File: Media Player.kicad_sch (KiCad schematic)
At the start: 40 parts, among them J1 PH2.0, J2 MEM2075-00-140-01-A, J3 USB_C_Receptacle_USB2.0_14P, SW1 BOOT, SW2 RESET, SW3 SW_Push, SW4 SW_Push, SW5 SW_Push, SW6 SW_Push, SW7 SW_SPST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

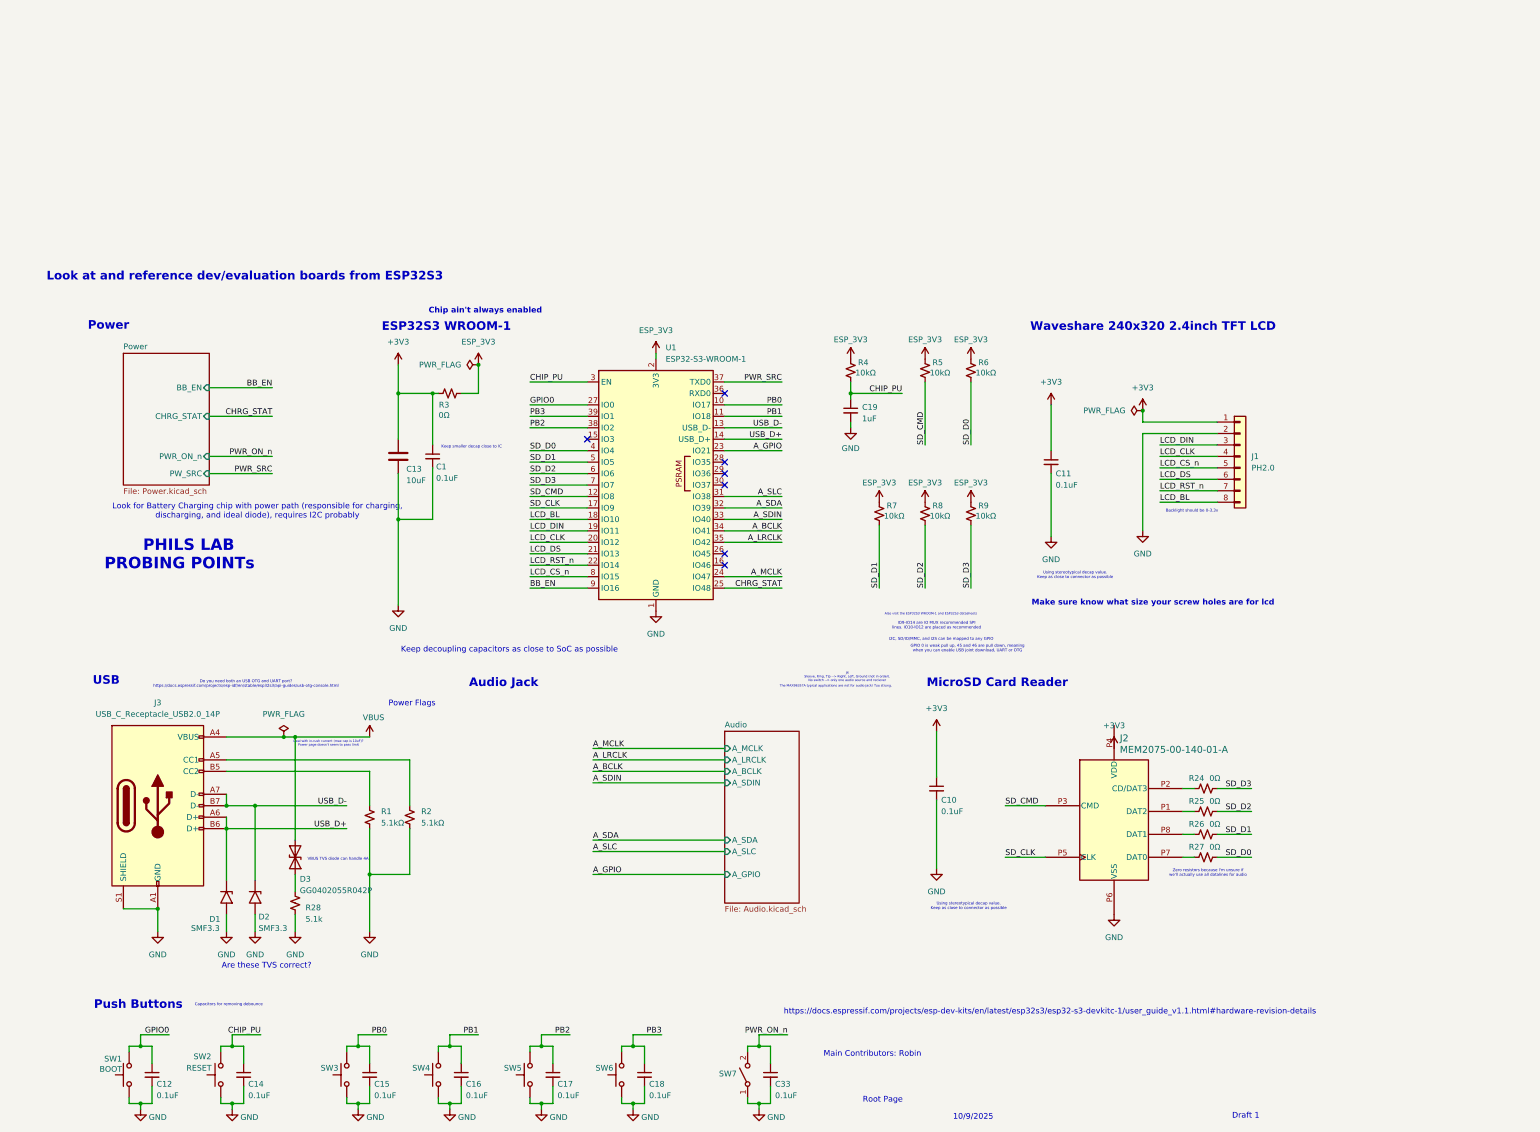
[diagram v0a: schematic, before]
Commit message: Draft 2 Revision 2
Footprints still not all assigned.

Added: Test points, zero resistors, battery voltage monitor IC, PTC and zener surge protection on VBUS, UART connector

Changed: rerouted some signals, removed zener and resistor for reverse pol bat protection
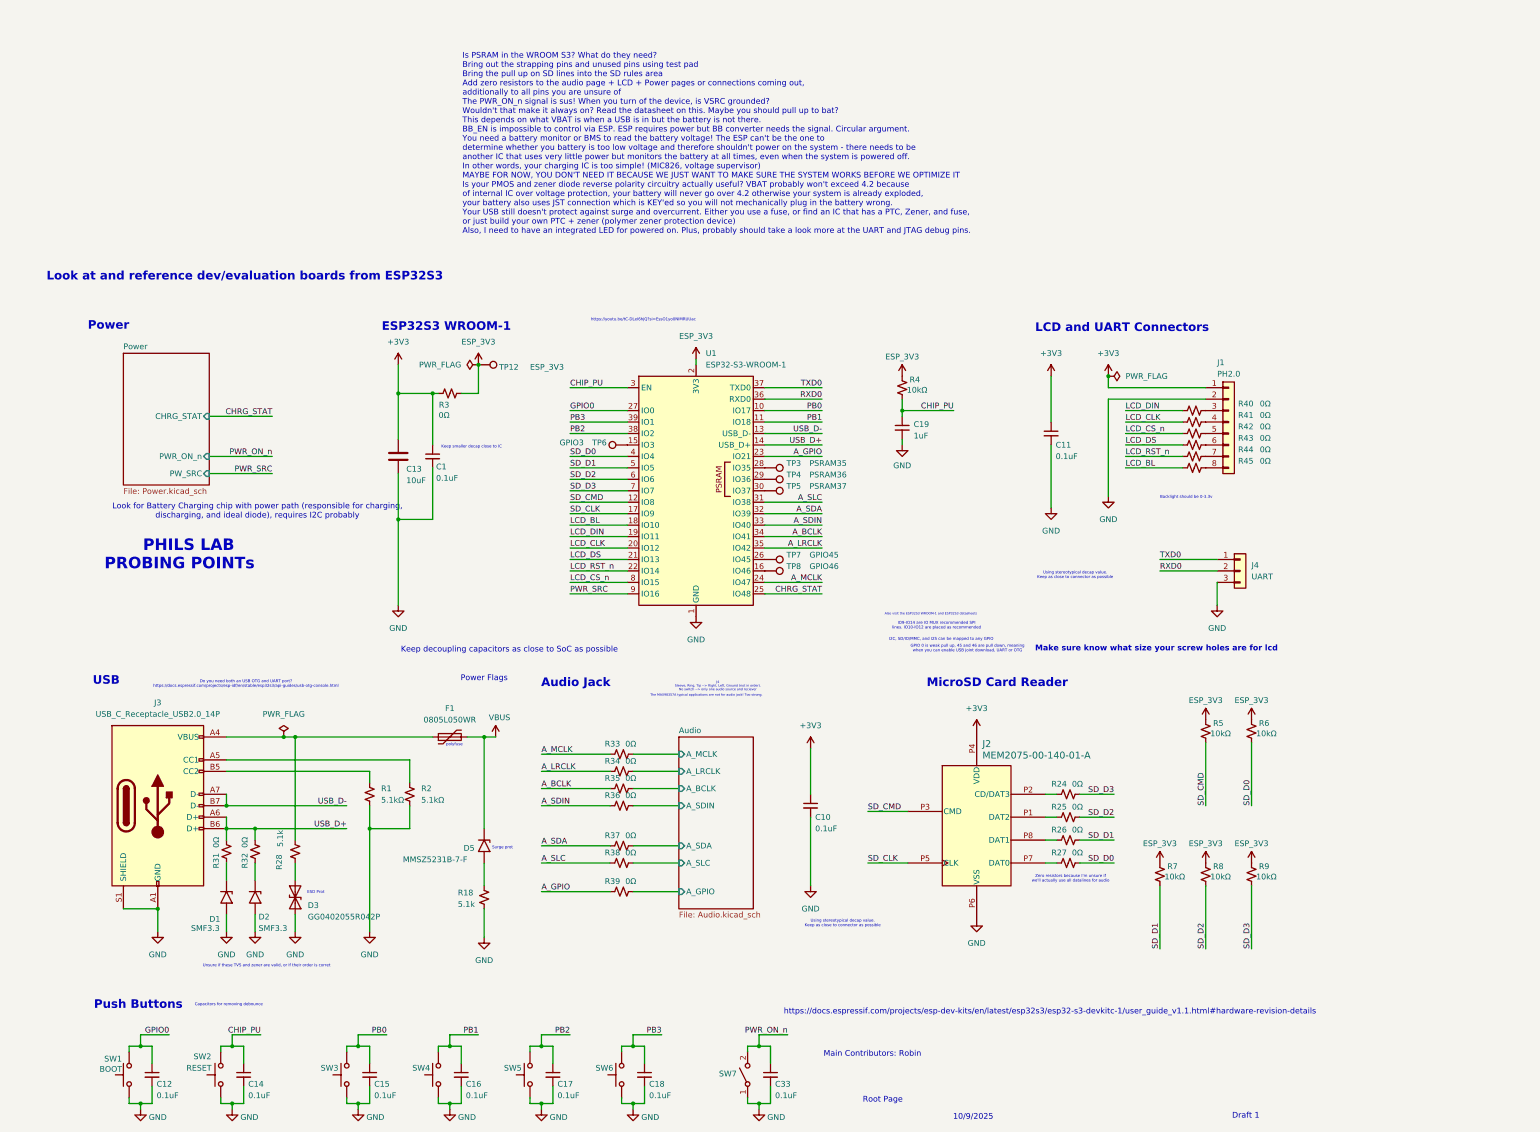
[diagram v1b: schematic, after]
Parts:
- added D5: MMSZ5231B-7-F, Diode_SMD:D_SMF, symbol Diode:SMF33A
- added F1: 0805L050WR, symbol Device:Polyfuse
- added J4: UART, symbol Connector_Generic:Conn_01x03
- added R18: 5.1k, symbol Device:R_Small_US
- added R31, R32, R33, R34, R35, R36, R37, R38, R39, R40, R41, R42, R43, R44, R45: 0Ω, Resistor_SMD:R_0805_2012Metric, symbol Device:R_Small_US
- added TP12: ESP_3V3, symbol Connector:TestPoint
- added TP3: PSRAM35, symbol Connector:TestPoint
- added TP4: PSRAM36, symbol Connector:TestPoint
- added TP5: PSRAM37, symbol Connector:TestPoint
- added TP6: GPIO3, symbol Connector:TestPoint
- added TP7: GPIO45, symbol Connector:TestPoint
- added TP8: GPIO46, symbol Connector:TestPoint
- R28: footprint (none) -> Resistor_SMD:R_0805_2012Metric
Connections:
- net BB_EN is gone; now on net PWR_SRC: U1.9 (IO16)
- net +3V3: now also J2.P4 (VDD)
- net A_BCLK: now also R35.1
- net A_GPIO: now also R39.1
- net A_LRCLK: now also R34.1
- net A_MCLK: now also R33.1
- net A_SDA: now also R37.1
- net A_SDIN: now also R36.1
- net A_SLC: now also R38.1
- net ESP_3V3: now also TP12.1
- net GND: now also D3.1 (A1), J4.3 (Pin_3), R18.2; no longer R28.2
- net LCD_BL: now also R45.1; no longer J1.8 (Pin_8)
- net LCD_CLK: now also R41.1; no longer J1.4 (Pin_4)
- net LCD_CS_n: now also R42.1; no longer J1.5 (Pin_5)
- net LCD_DIN: now also R40.1; no longer J1.3 (Pin_3)
- net LCD_DS: now also R43.1; no longer J1.6 (Pin_6)
- net LCD_RST_n: now also R44.1; no longer J1.7 (Pin_7)
- net PWR_SRC: no longer U1.37 (TXD0)
- net USB_D+: now also R31.2, R32.2; no longer D1.1 (A1)
- net USB_D-: no longer D2.1 (A1)
- net VBUS: now also D5.1 (A1), F1.2; no longer D3.2 (A2), J3.A4 (VBUS), J3.A9 (VBUS), J3.B4 (VBUS), J3.B9 (VBUS)
- net at R28.1: now also J3.A4 (VBUS), J3.A9 (VBUS), J3.B4 (VBUS), J3.B9 (VBUS), F1.1; no longer D3.1 (A1)
- net at U1.15 (IO3): now also TP6.1
- net at U1.16 (IO46): now also TP8.1
- net at U1.26 (IO45): now also TP7.1
- net at U1.28 (IO35): now also TP3.1
- net at U1.29 (IO36): now also TP4.1
- net at U1.30 (IO37): now also TP5.1
- net RXD0: now reaches U1.36 (RXD0)
- net RXD0: now also J4.2 (Pin_2)
- new net: J1.5 (Pin_5), R42.2
- new net: J1.6 (Pin_6), R43.2
- new net: D3.2 (A2), R28.2
- new net: J1.4 (Pin_4), R41.2
- new net: D5.2 (A2), R18.1
- new net: D1.1 (A1), R31.1
- new net: J1.3 (Pin_3), R40.2
- new net: J1.7 (Pin_7), R44.2
- new net: J1.8 (Pin_8), R45.2
- new net: D2.1 (A1), R32.1
- new net Audio/A_BCLK: R35.2
- new net Audio/A_GPIO: R39.2
- new net Audio/A_LRCLK: R34.2
- new net Audio/A_MCLK: R33.2
- new net Audio/A_SDA: R37.2
- new net Audio/A_SDIN: R36.2
- new net Audio/A_SLC: R38.2
- new net TXD0: J4.1 (Pin_1), U1.37 (TXD0)
- no-connect marks 7 -> 0
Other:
- sheet Power ports: added none; removed BB_EN
- note added: "ESD Prot"
- note added: "Is PSRAM in the WROOM S3? What do they need? Bring out the strapping pins and unused pins using test pad Bring the pull up on SD lines into the SD rules area Add zero resistors to the audio page + LCD + Power pages or connections coming out, additionally to all pins you are unsure of The PWR_ON_n signal is sus! When you turn of the device, is VSRC grounded? Wouldn't that make it always on? Read t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"
- note added: "LCD and UART Connectors"
- note added: "Surge prot"
- note added: "Unsure if these TVS and zener are valid, or if their order is corret"
- note added: "https://youtu.be/tC-DLeI6hjQ?si=EssO1yo0NIMRUUac"
- note added: "polyfuse"
- note removed: "Are these TVS correct?"
- note removed: "Chip ain't always enabled"
- note removed: "Deal with in-rush current (max cap is 10uF)? Power page doesn't seem to pass limit"
- note removed: "VBUS TVS diode can handle 4A."
- note removed: "Waveshare 240x320 2.4inch TFT LCD"
- moved on the sheet: C10, C11, C19, D3, J1, J2, R1, R2, R24, R25, R26, R27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

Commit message: Remaining Footprint Added
Beware of footprints that come from online but do not match the kicad libraries - the pins might be mapped wrong!
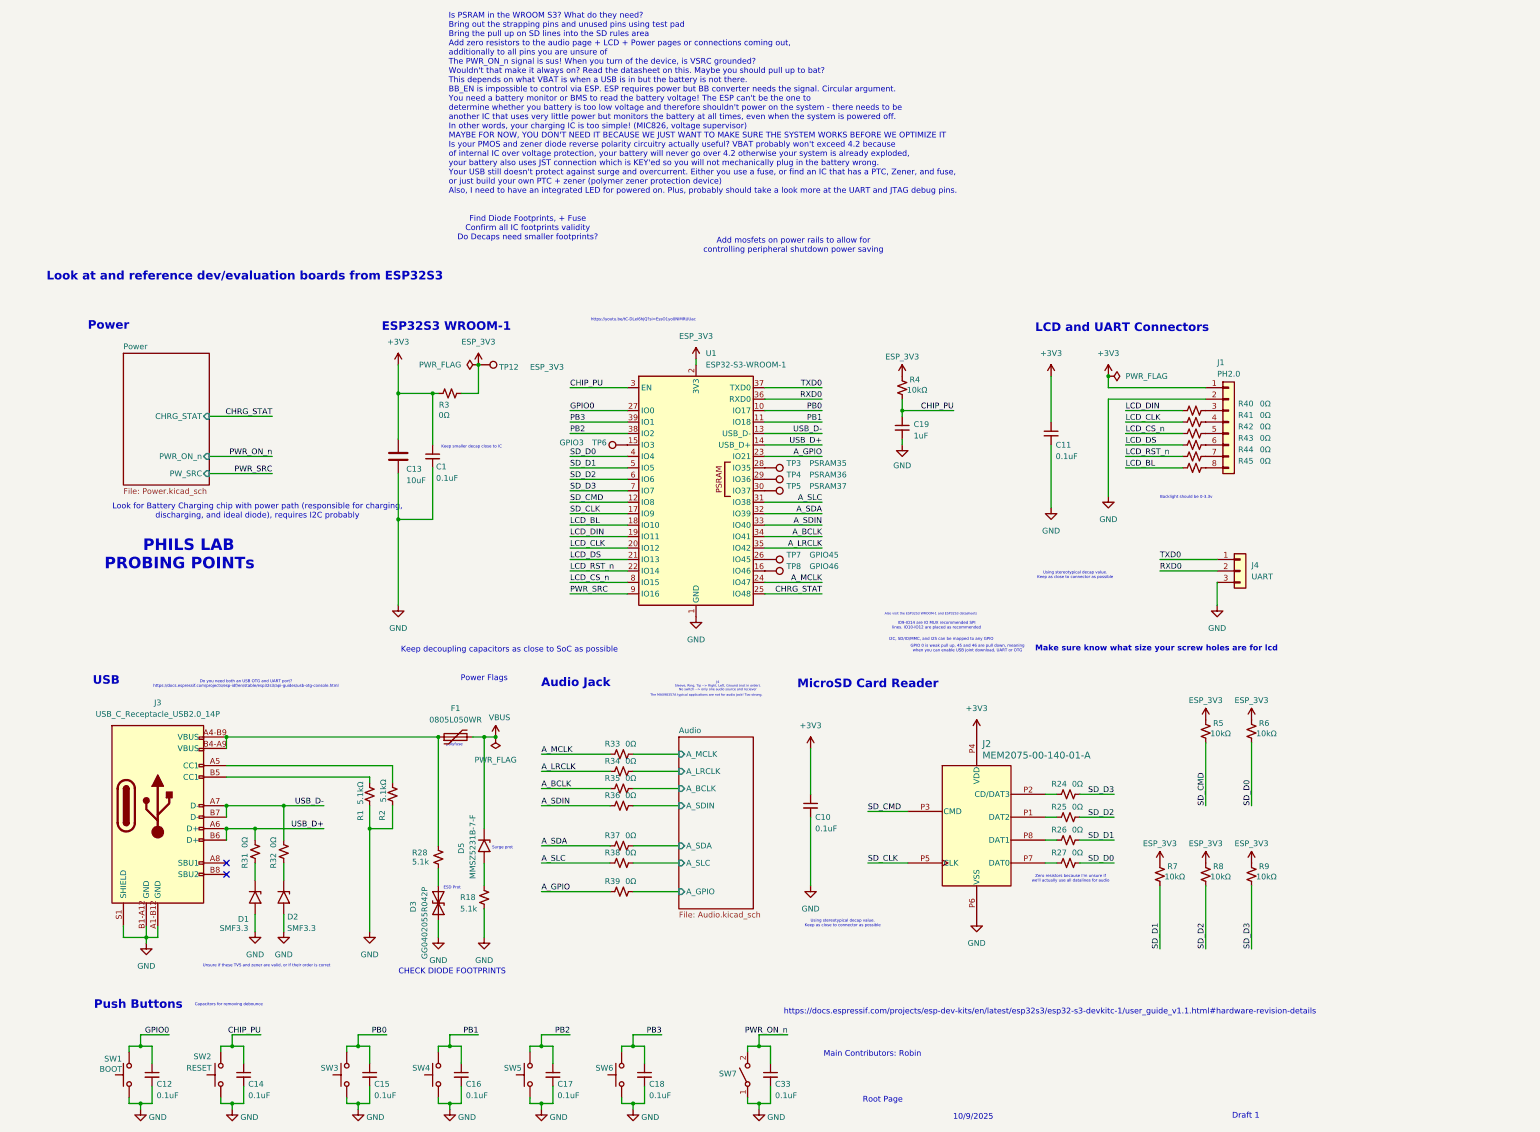
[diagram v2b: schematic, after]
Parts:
- D1, D2: footprint Diode_SMD:D_SMF -> Diode_SMD:D_SOD-123F
- D3: footprint Diode_THT:D_DO-201AE_P15.24mm_Horizontal -> Diode_SMD:D_0805_2012Metric_Pad1.15x1.40mm_HandSolder
- D5: footprint Diode_SMD:D_SMF -> Diode_SMD:D_SOD-323
- F1: footprint (none) -> Diode_SMD:D_0805_2012Metric_Pad1.15x1.40mm_HandSolder
- J3: footprint Connector_USB:USB_C_Receptacle_HRO_TYPE-C-31-M-12 -> Footprints:USB_C_12402012E212A_AMP; symbol Connector:USB_C_Receptacle_USB2.0_14P -> Connector:USB_C_Receptacle_USB2.0_16P
- J4: footprint (none) -> Connector_JST:JST_PH_B3B-PH-K_1x03_P2.00mm_Vertical
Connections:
- net GND: now also J3.A1-B12 (GND), J3.B1-A12 (GND); no longer J3.A1 (GND)
- net USB_D+: no longer R32.2
- net USB_D-: now also R32.2
- net at F1.1, J3.A9 (VBUS), J3.B4 (VBUS)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: now also J3.A4-B9 (VBUS), J3.B4-A9 (VBUS); no longer J3.A4 (VBUS)
- no-connect marks 0 -> 2
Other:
- note added: "Add mosfets on power rails to allow for controlling peripheral shutdown power saving"
- note added: "CHECK DIODE FOOTPRINTS"
- note added: "Find Diode Footprints, + Fuse Confirm all IC footprints validity Do Decaps need smaller footprints?"
- moved on the sheet: D1, D2, D3, F1, R2, R28, R31, R32

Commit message: Components Placed on Layout
Added Power Management PMOS, Assigned missing footprints
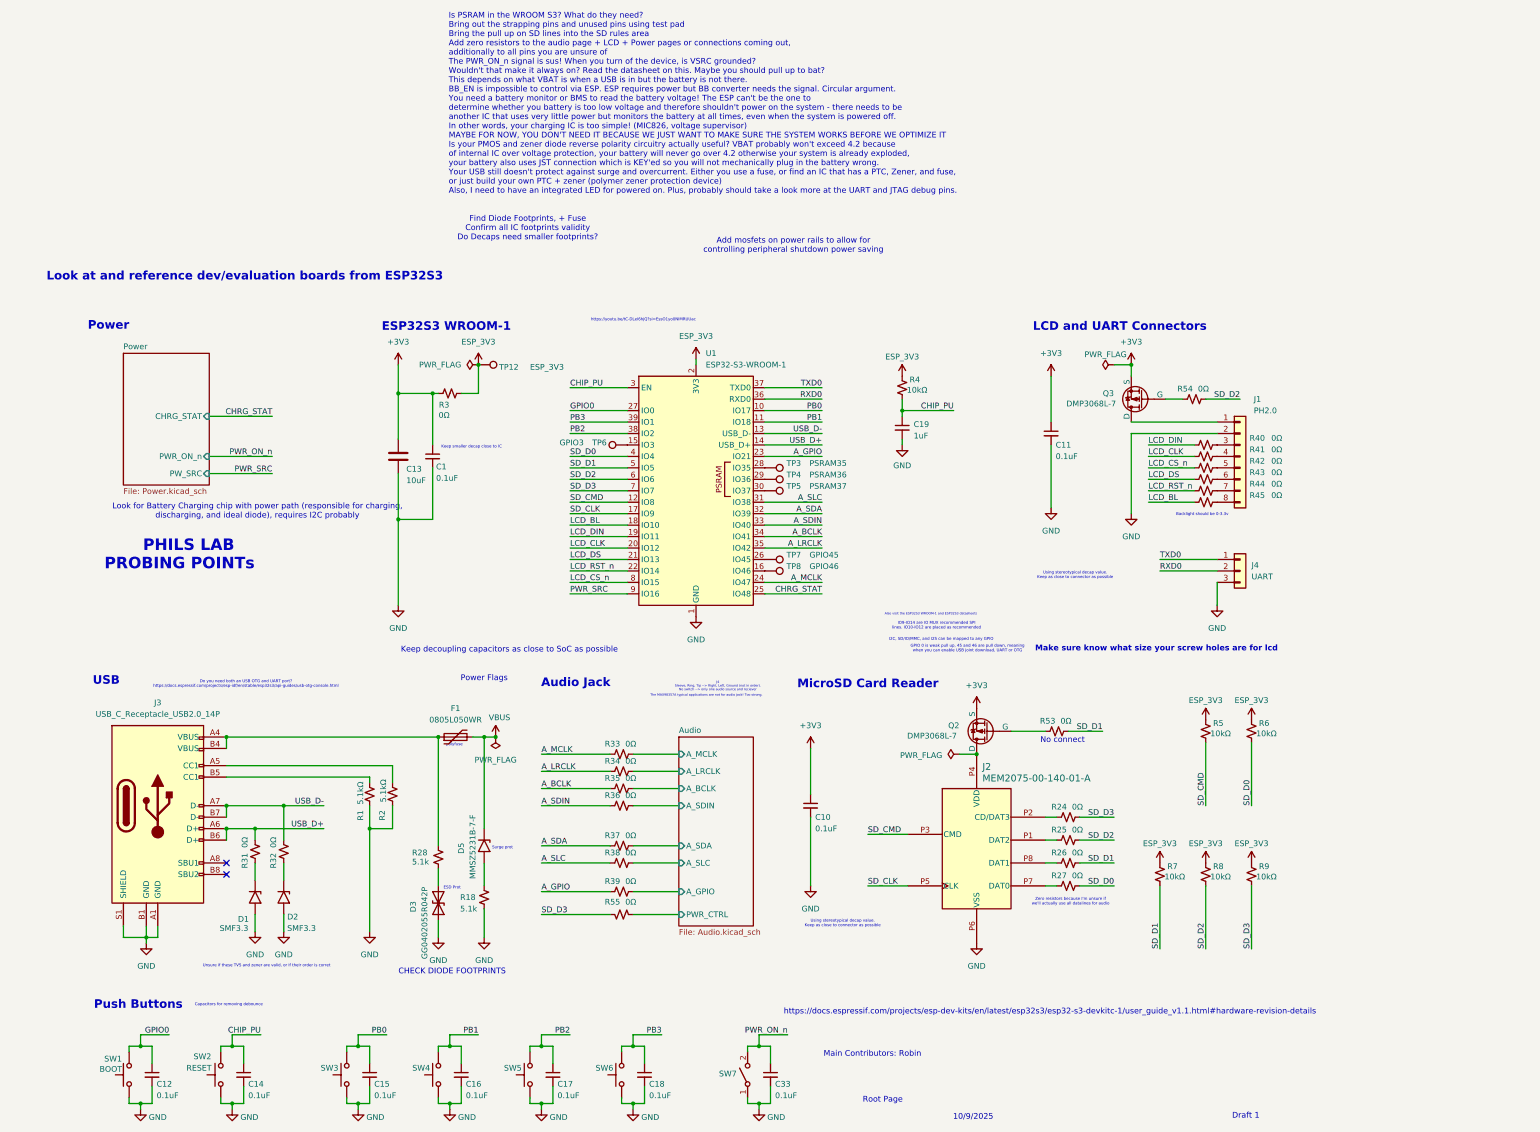
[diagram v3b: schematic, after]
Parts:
- added Q2, Q3: DMP3068L-7, Package_TO_SOT_SMD:SOT-23-3, symbol Simulation_SPICE:PMOS
- added R53, R54, R55: 0Ω, Resistor_SMD:R_0805_2012Metric, symbol Device:R_Small_US
- R18, R24, R25, R26, R27: footprint (none) -> Resistor_SMD:R_0805_2012Metric
- TP12, TP3, TP4, TP5, TP6, TP7, TP8: footprint (none) -> TestPoint:TestPoint_Pad_1.5x1.5mm
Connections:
- net +3V3: now also Q2.3 (S), Q3.3 (S); no longer J1.1 (Pin_1), J2.P4 (VDD)
- net GND: now also J3.A1 (GND); no longer J3.A1-B12 (GND), J3.B1-A12 (GND)
- net SD_D1: now also R53.2
- net SD_D2: now also R54.2
- net SD_D3: now also R55.2
- net at F1.1, J3.A9 (VBUS), J3.B4 (VBUS)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: now also J3.A4 (VBUS); no longer J3.A4-B9 (VBUS), J3.B4-A9 (VBUS)
- new net: J2.P4 (VDD), Q2.1 (D)
- new net: Q2.2 (G), R53.1
- new net: Q3.2 (G), R54.1
- new net: J1.1 (Pin_1), Q3.1 (D)
- new net Audio/PWR_CTRL: R55.1
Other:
- sheet Audio ports: added PWR_CTRL; removed none
- note added: "No connect"
- moved on the sheet: J1, J2, J3, R24, R25, R26, R27, R40, R41, R42, R43, R44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
